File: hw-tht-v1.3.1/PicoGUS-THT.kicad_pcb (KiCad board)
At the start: 2 copper layers, 103.7 x 99.8 mm, 88 parts, among them J1 IRQDMA_JP, J10 GY-PCM5102, J11 USB-A, J3 Bus_ISA_8bit, J5 SJ1-3535NG, J6 UART_TX, J7 USB power jumper, J8 SJ1-3535NG-GR, J9 Waveblaster, U1 Pico, U10 74AHCT126, U11 NE5532, U12 USBLC6-2SC6, U2 74AHC244, U3 SN74CB3T3257, U4 SN74CB3T3257, U5 74AHC14, U6 74AHC00, U7 74AHC00, U8 APS6404L-3SQR-SN, U9 PCM5100A

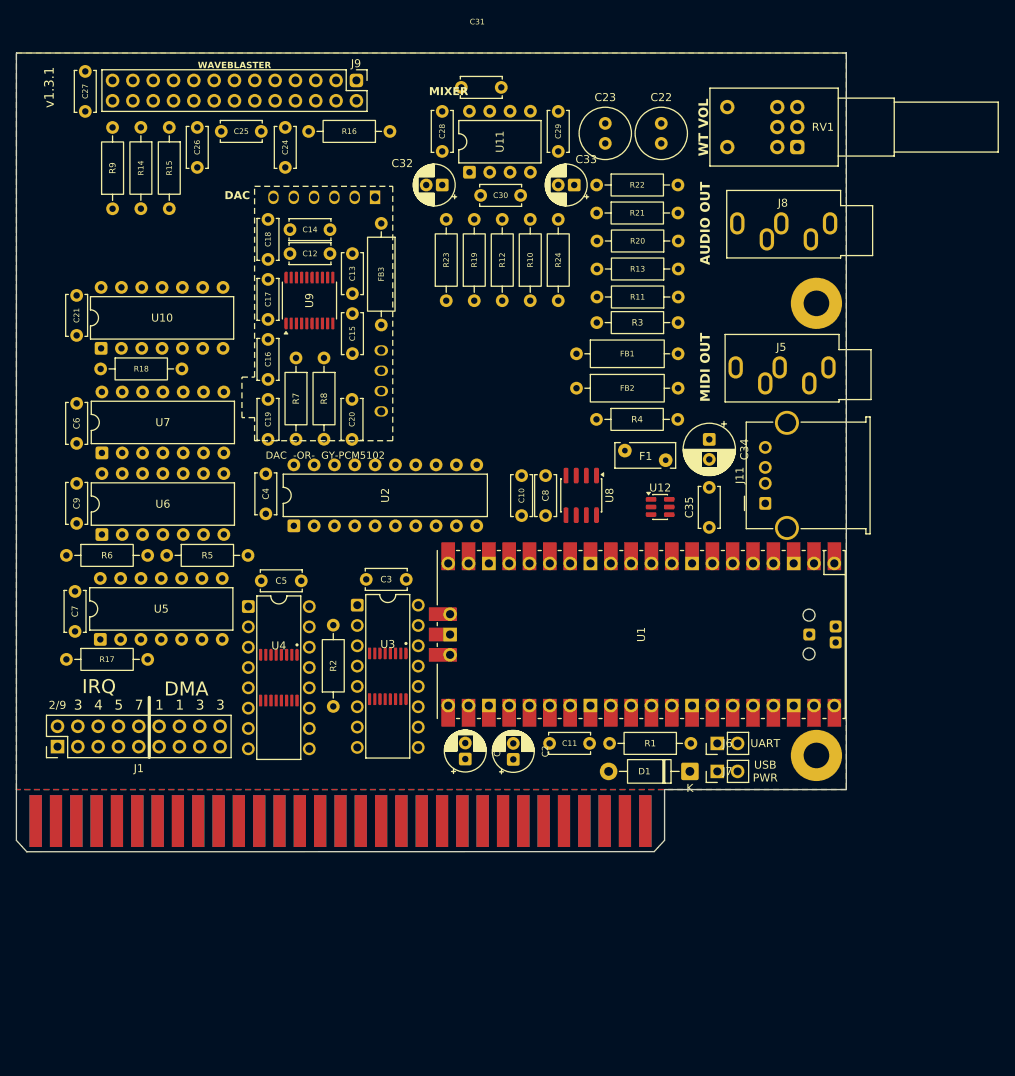
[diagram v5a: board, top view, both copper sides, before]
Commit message: THT rev B: take 2 placement fixes from the review (bracket window, J11 flange, C32)
- RV1/J8 swapped: RV1's bushing was above the PC slot opening
- J11 moved 1.36 mm in so its flange stays behind the bracket; C34/F1/R4 nudged
- C32 out from under the daughterboard; R17/U5 and J6/J7 overlaps fixed
- R19/R20 turned (summing nodes at U11), C8 next to U8, R2 horizontal, C1/C2
- README: bracket drilling table, layout status; socket BOM: U3/U4 under the daughterboard

Co-Authored-By: Claude Opus 5.5 <noreply@anthropic.com>
Claude-Session: https://claude.ai/code/session_011utN3x8yYUNDvkpGCEq5yD
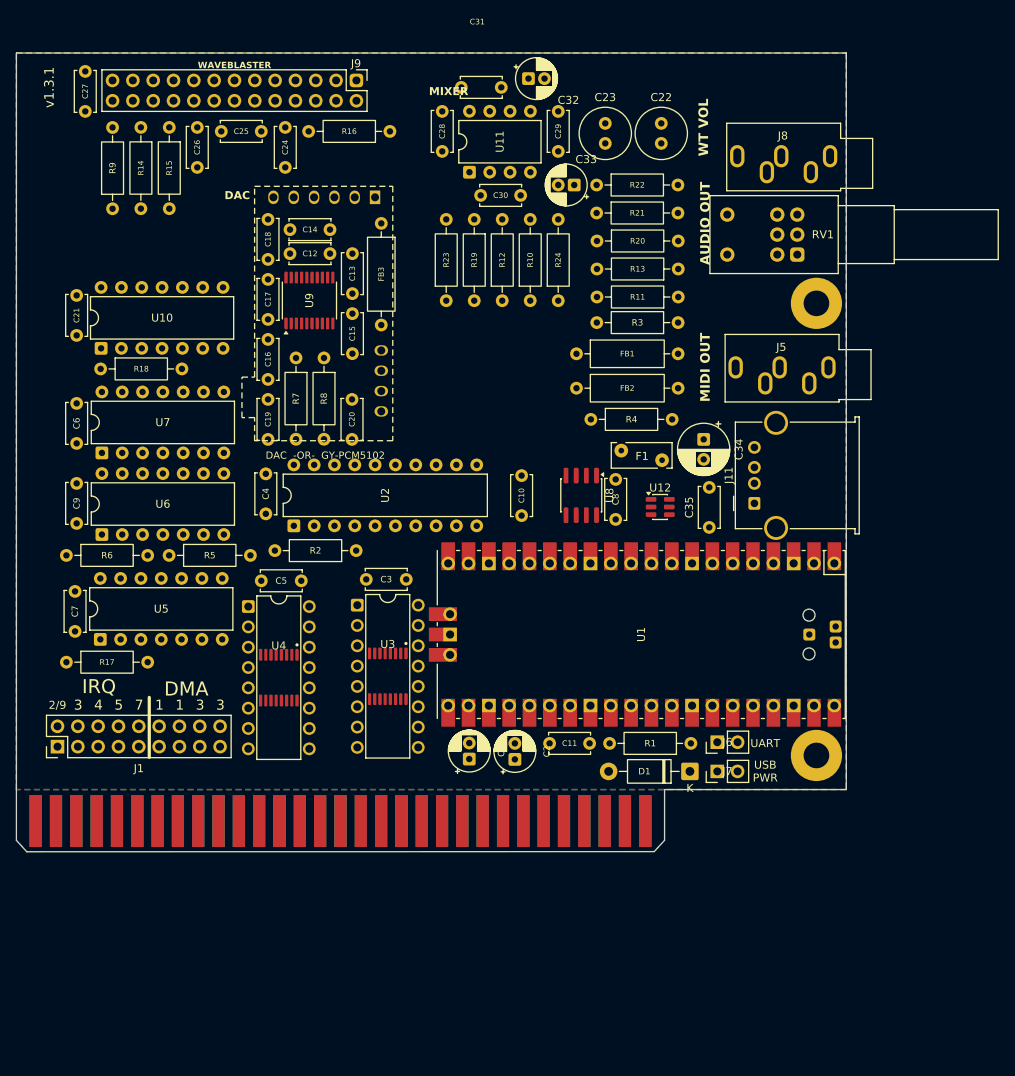
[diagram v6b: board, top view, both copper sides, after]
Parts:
- moved R2 19.7 mm to (158.9, 98.4), turned to 180 degrees
- moved C32 17.1 mm to (180.4, 39.4), turned to 0 degrees
- moved RV1 13.4 mm to (214.0, 61.4)
- moved R19 10.2 mm to (173.6, 57.0), turned to -90 degrees
- moved R20 10.2 mm to (189.0, 59.7), turned to 0 degrees
- moved C8 8.77 mm to (191.3, 94.5)
- moved J8 8.40 mm to (218.1, 49.1)
- moved J11 1.36 mm to (208.6, 92.5)
- moved R4 0.70 mm to (188.2, 82.0)
- moved C34 0.70 mm to (202.3, 84.5)
- moved C1 0.50 mm to (173.0, 124.5)
- moved F1 0.45 mm to (192.0, 85.9)
- moved R17 0.35 mm to (122.6, 112.3)
- moved R5 0.30 mm to (135.5, 99.0)
- moved C2 0.20 mm to (178.7, 124.5)
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
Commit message: THT rev B: take 2 routed (DRC clean with schematic parity)
- Freerouting after locked pre-routes: IRQ2 and D5 along the finger corridor, USB D+/D- between
  the Pico's micro-USB shell holes, U9 GND/VNEG/XSMT stubs
- signal tracks 0.2 mm, signal vias 0.6/0.3 mm (power/GND classes unchanged)
- GND pours on both layers + stitching vias; rule areas for the front logo and under the flat Pico
- silkscreen: labels/references off pads, USB label, WT VOL/AUDIO OUT swapped with the parts,
  back artwork re-cut around the pads and vias, back texts back on the board

Co-Authored-By: Claude Opus 5.5 <noreply@anthropic.com>
Claude-Session: https://claude.ai/code/session_011utN3x8yYUNDvkpGCEq5yD
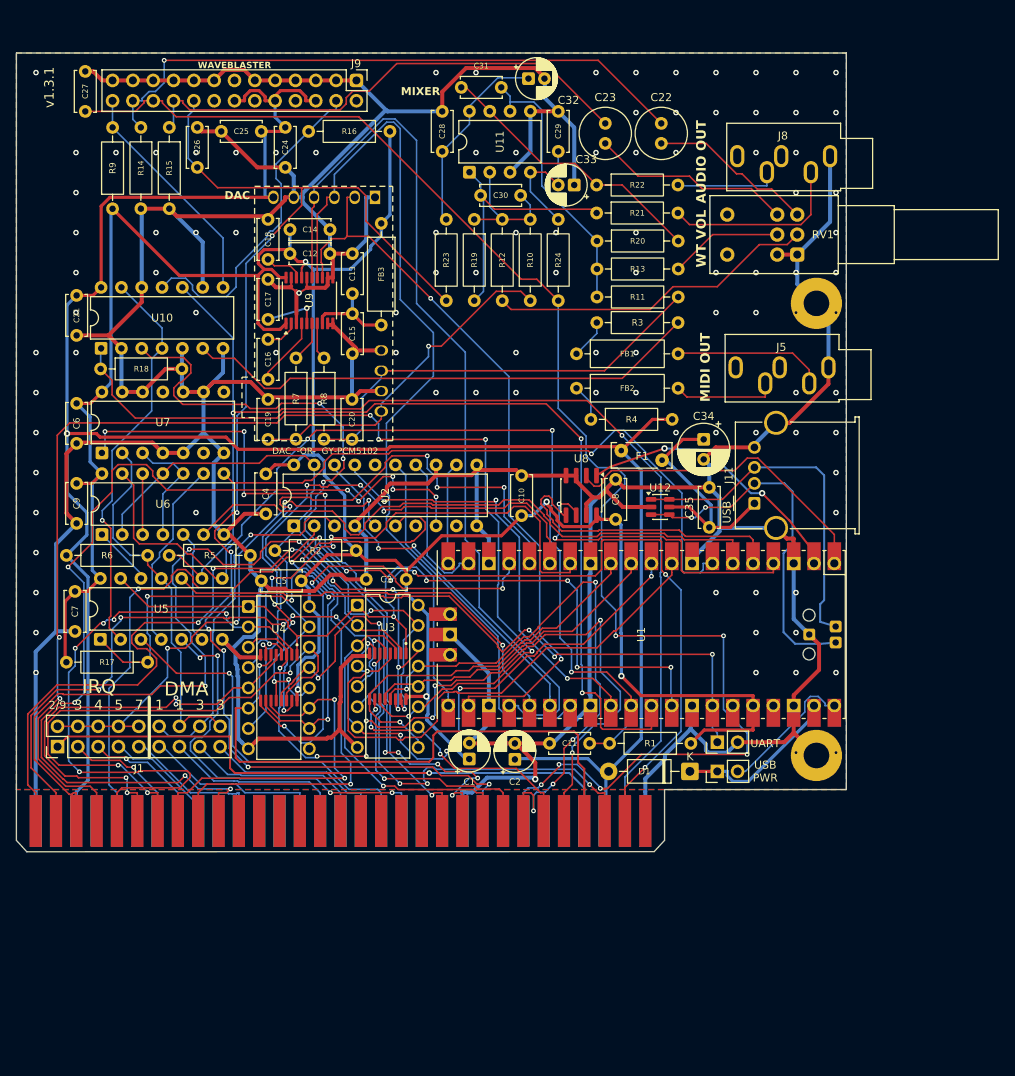
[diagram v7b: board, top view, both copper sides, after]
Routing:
- net GND: track 0.00 -> 776.2 mm, vias 0 -> 101
- net +3V3: track 0.00 -> 334.2 mm, vias 0 -> 5
- net +5V: track 0.00 -> 275.9 mm, vias 0 -> 1
- net -12V: track 0.00 -> 184.7 mm, vias 0 -> 6
- net +12V: track 0.00 -> 167.0 mm, vias 0 -> 7
- net A3: track 0.00 -> 164.2 mm, vias 0 -> 7
- net RESET: track 0.00 -> 149.2 mm, vias 0 -> 2
- net D7: track 0.00 -> 127.1 mm, vias 0 -> 8
- net RUN: track 0.00 -> 124.5 mm, vias 0 -> 3
- net A9: track 0.00 -> 123.5 mm, vias 0 -> 9
- net ~{RI/OCHRDY}: track 0.00 -> 116.2 mm, vias 0 -> 2
- net LRCK: track 0.00 -> 114.5 mm
- net A2: track 0.00 -> 110.0 mm, vias 0 -> 7
- net UART_TX: track 0.00 -> 108.4 mm, vias 0 -> 6
- net DIN: track 0.00 -> 105.4 mm
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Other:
- board text added: "USB"

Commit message: THT rev B: fixes from the routed-board review
- D2 via out of the gold-finger area; J3 finger mask opening starts at y 129.6 on this board
  so the vias above the fingers are tented (board-only edit of the shared footprint)
- J11 shield pad 2.8 mm on F.Cu (0.38 mm to Pico SPI_SCK); H2 mask margin -0.3 mm
- C1/C2 0.5 mm right (daughterboard corner); -12V off a Pico test pad; ~SPI_CS nudged;
  MIDI drive re-routed away from AUDIO_R with GND vias
- silk: all text >= 0.8 mm / 0.15 mm, LINE OUT label, REAR/C32/C33 labels moved, title block
- README: ENIG required for gold fingers, rev B bracket, layout notes; BOM: J11 cut-out 13.6 x 6.2 mm

DRC with schematic parity: 0 errors, 0 unconnected.

Co-Authored-By: Claude Opus 5.5 <noreply@anthropic.com>
Claude-Session: https://claude.ai/code/session_011utN3x8yYUNDvkpGCEq5yD
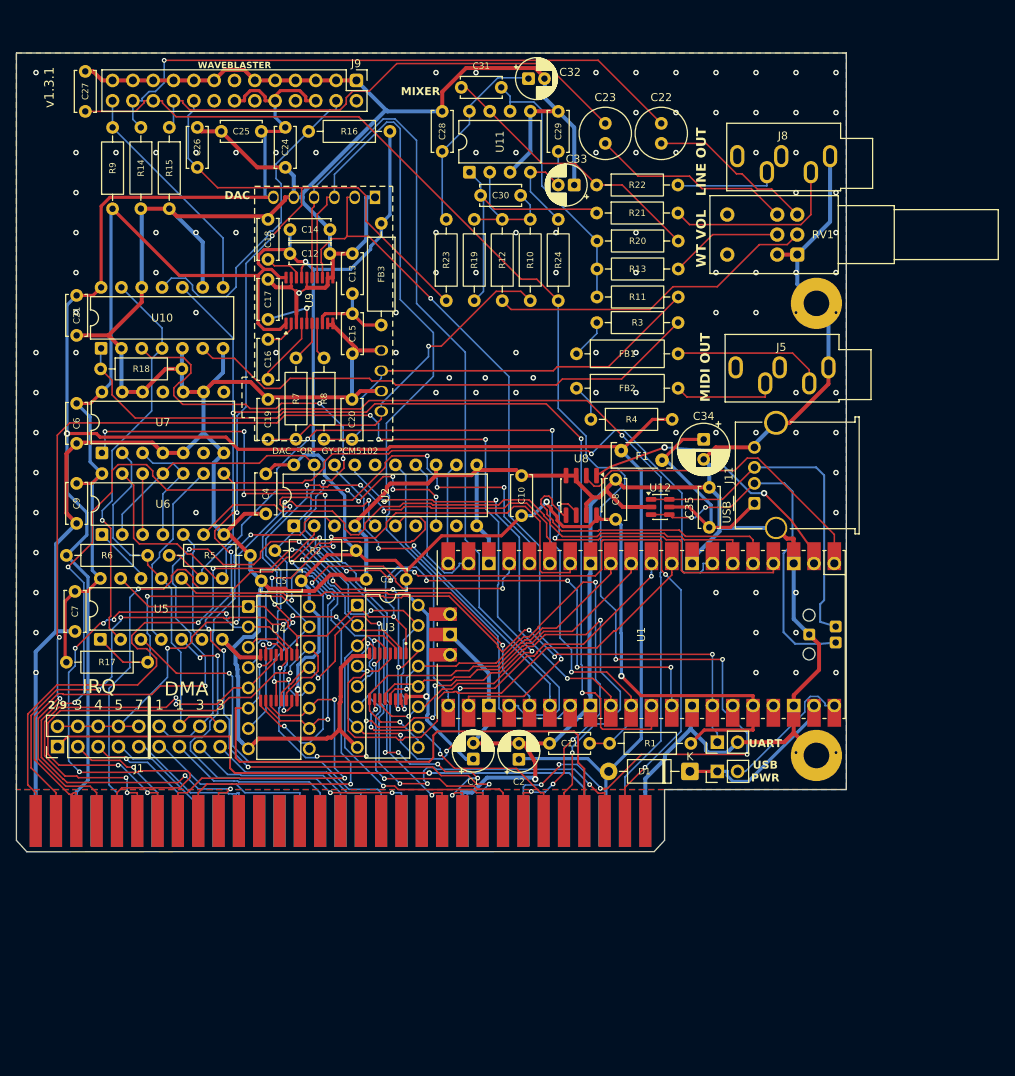
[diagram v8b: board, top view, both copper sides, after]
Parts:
- moved C1 0.50 mm to (173.5, 124.5)
- moved C2 0.50 mm to (179.2, 124.5)
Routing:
- net D2: track 72.8 -> 68.8 mm
- net GND: track 776.2 -> 775.3 mm, vias 101 -> 104
- net Net-(R3-Pad1): track 64.9 -> 65.6 mm
- net -12V: track 184.7 -> 185.3 mm
- net +5V: track 275.9 -> 275.4 mm
- net +3V3: track 334.2 -> 334.7 mm
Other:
- board text added: "LINE OUT"
- board text removed: "AUDIO OUT"
